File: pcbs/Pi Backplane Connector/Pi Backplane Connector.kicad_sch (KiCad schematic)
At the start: 66 parts, among them J1001 Conn_02x20_Odd_Even, J1002 Conn_02x20_Odd_Even

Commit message: Some routing
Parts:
- added D1033, D1034, D1035, D1036, D1037, D1038, D1039, D1040, D1041, D1042, D1043, D1044, D1045, D1046, D1047, D1048: White, LED_SMD:LED_0603_1608Metric, symbol Device:LED
- added R1033, R1034, R1035, R1036, R1037, R1038, R1039, R1040, R1041, R1042, R1043, R1044, R1045, R1046, R1047, R1048: 4.7k, Resistor_SMD:R_0603_1608Metric, symbol Device:R
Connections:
- net C0: now also J1002.1 (Pin_1), R1033.1; no longer J1002.17 (Pin_17)
- net C1: now also J1002.2 (Pin_2), R1034.1; no longer J1002.18 (Pin_18)
- net C10: now also J1002.11 (Pin_11), R1043.1; no longer J1002.27 (Pin_27)
- net C11: now also J1002.12 (Pin_12), R1044.1; no longer J1002.28 (Pin_28)
- net C12: now also J1002.13 (Pin_13), R1045.1; no longer J1002.29 (Pin_29)
- net C13: now also J1002.14 (Pin_14), R1046.1; no longer J1002.30 (Pin_30)
- net C14: now also J1002.15 (Pin_15), R1047.1; no longer J1002.31 (Pin_31)
- net C15: now also J1002.16 (Pin_16), R1048.1; no longer J1002.32 (Pin_32)
- net C2: now also J1002.3 (Pin_3), R1035.1; no longer J1002.19 (Pin_19)
- net C3: now also J1002.4 (Pin_4), R1036.1; no longer J1002.20 (Pin_20)
- net C4: now also J1002.5 (Pin_5), R1037.1; no longer J1002.21 (Pin_21)
- net C5: now also J1002.6 (Pin_6), R1038.1; no longer J1002.22 (Pin_22)
- net C6: now also J1002.7 (Pin_7), R1039.1; no longer J1002.23 (Pin_23)
- net C7: now also J1002.8 (Pin_8), R1040.1; no longer J1002.24 (Pin_24)
- net C8: now also J1002.9 (Pin_9), R1041.1; no longer J1002.25 (Pin_25)
- net C9: now also J1002.10 (Pin_10), R1042.1; no longer J1002.26 (Pin_26)
- net GND: now also D1033.1 (K), D1034.1 (K), D1035.1 (K), D1036.1 (K), D1037.1 (K), D1038.1 (K), D1039.1 (K), D1040.1 (K), D1041.1 (K), D1042.1 (K), D1043.1 (K), D1044.1 (K), D1045.1 (K), D1046.1 (K), D1047.1 (K), D1048.1 (K)
- net I0: now also J1002.17 (Pin_17); no longer J1002.1 (Pin_1)
- net I1: now also J1002.18 (Pin_18); no longer J1002.2 (Pin_2)
- net I10: now also J1002.27 (Pin_27); no longer J1002.11 (Pin_11)
- net I11: now also J1002.28 (Pin_28); no longer J1002.12 (Pin_12)
- net I12: now also J1002.29 (Pin_29); no longer J1002.13 (Pin_13)
- net I13: now also J1002.30 (Pin_30); no longer J1002.14 (Pin_14)
- net I14: now also J1002.31 (Pin_31); no longer J1002.15 (Pin_15)
- net I15: now also J1002.32 (Pin_32); no longer J1002.16 (Pin_16)
- net I2: now also J1002.19 (Pin_19); no longer J1002.3 (Pin_3)
- net I3: now also J1002.20 (Pin_20); no longer J1002.4 (Pin_4)
- net I4: now also J1002.21 (Pin_21); no longer J1002.5 (Pin_5)
- net I5: now also J1002.22 (Pin_22); no longer J1002.6 (Pin_6)
- net I6: now also J1002.23 (Pin_23); no longer J1002.7 (Pin_7)
- net I7: now also J1002.24 (Pin_24); no longer J1002.8 (Pin_8)
- net I8: now also J1002.25 (Pin_25); no longer J1002.9 (Pin_9)
- net I9: now also J1002.26 (Pin_26); no longer J1002.10 (Pin_10)
- new net: D1034.2 (A), R1034.2
- new net: D1048.2 (A), R1048.2
- new net: D1035.2 (A), R1035.2
- new net: D1037.2 (A), R1037.2
- new net: D1033.2 (A), R1033.2
- new net: D1045.2 (A), R1045.2
- new net: D1043.2 (A), R1043.2
- new net: D1039.2 (A), R1039.2
- new net: D1036.2 (A), R1036.2
- new net: D1044.2 (A), R1044.2
- new net: D1047.2 (A), R1047.2
- new net: D1041.2 (A), R1041.2
- new net: D1040.2 (A), R1040.2
- new net: D1042.2 (A), R1042.2
- new net: D1046.2 (A), R1046.2
- new net: D1038.2 (A), R1038.2
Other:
- sheet Inputs ports: added B[0..15], C[0..15], I[0..15], ~{IN_{LOBD}}; removed none

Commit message: Doing some routing
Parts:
- added D1049, D1050, D1051, D1052, D1053, D1054, D1055, D1056, D1057, D1058, D1059, D1060, D1061, D1062, D1063, D1064: Green, LED_SMD:LED_0603_1608Metric, symbol Device:LED
- added R1049, R1050, R1051, R1052, R1053, R1054, R1055, R1056, R1057, R1058, R1059, R1060, R1061, R1062, R1063, R1064: 4.7k, Resistor_SMD:R_0603_1608Metric, symbol Device:R
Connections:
- net GND: now also D1049.1 (K), D1050.1 (K), D1051.1 (K), D1052.1 (K), D1053.1 (K), D1054.1 (K), D1055.1 (K), D1056.1 (K), D1057.1 (K), D1058.1 (K), D1059.1 (K), D1060.1 (K), D1061.1 (K), D1062.1 (K), D1063.1 (K), D1064.1 (K)
- net I0: now also R1049.1
- net I1: now also R1050.1
- net I10: now also R1059.1
- net I11: now also R1060.1
- net I12: now also R1061.1
- net I13: now also R1062.1
- net I14: now also R1063.1
- net I15: now also R1064.1
- net I2: now also R1051.1
- net I3: now also R1052.1
- net I4: now also R1053.1
- net I5: now also R1054.1
- net I6: now also R1055.1
- net I7: now also R1056.1
- net I8: now also R1057.1
- net I9: now also R1058.1
- new net: D1055.2 (A), R1055.2
- new net: D1057.2 (A), R1057.2
- new net: D1062.2 (A), R1062.2
- new net: D1054.2 (A), R1054.2
- new net: D1061.2 (A), R1061.2
- new net: D1064.2 (A), R1064.2
- new net: D1051.2 (A), R1051.2
- new net: D1063.2 (A), R1063.2
- new net: D1060.2 (A), R1060.2
- new net: D1058.2 (A), R1058.2
- new net: D1049.2 (A), R1049.2
- new net: D1050.2 (A), R1050.2
- new net: D1053.2 (A), R1053.2
- new net: D1052.2 (A), R1052.2
- new net: D1056.2 (A), R1056.2
- new net: D1059.2 (A), R1059.2

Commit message: More connections, more routing
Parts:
- added D1065, D1066, D1067, D1068, D1069: Yellow, LED_SMD:LED_0603_1608Metric, symbol Device:LED
- added R1065, R1066, R1067, R1068, R1069: 4.7k, Resistor_SMD:R_0603_1608Metric, symbol Device:R
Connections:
- net GND: now also D1065.1 (K), D1066.1 (K), D1067.1 (K), D1068.1 (K), D1069.1 (K)
- net Cycle0: now reaches J1002.33 (Pin_33)
- net Cycle0: now also R1065.1
- net Cycle1: now reaches J1002.34 (Pin_34)
- net Cycle1: now also R1066.1
- net Cycle2: now reaches J1002.35 (Pin_35)
- net Cycle2: now also R1067.1
- net Cycle3: now reaches J1002.36 (Pin_36)
- net Cycle3: now also R1068.1
- net Cycle4: now reaches J1002.37 (Pin_37)
- net Cycle4: now also R1069.1
- new net: D1066.2 (A), R1066.2
- new net: D1067.2 (A), R1067.2
- new net: D1065.2 (A), R1065.2
- new net: D1068.2 (A), R1068.2
- new net: D1069.2 (A), R1069.2
- no-connect marks 0 -> 1
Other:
- sheet Inputs ports: added Cycle[0..4]; removed none
- sheet Outputs ports: added Cycle[0..4], DATA, RCLK, SRCLK, ~{Enable_{Cycle}}; removed none

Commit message: Connections and capacitors
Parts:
- added D1070, D1071: Yellow, LED_SMD:LED_0603_1608Metric, symbol Device:LED
- added R1070, R1071: 4.7k, Resistor_SMD:R_0603_1608Metric, symbol Device:R
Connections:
- net GND: now also D1070.1 (K), D1071.1 (K)
- net RESET: now reaches J1001.39 (Pin_39)
- net RESET: now also R1071.1
- net CLOCK: now reaches J1001.40 (Pin_40)
- net CLOCK: now also R1070.1
- new net: D1071.2 (A), R1071.2
- new net: D1070.2 (A), R1070.2
- no-connect marks 1 -> 5
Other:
- sheet Inputs ports: added CLOCK, RESET; removed none
- sheet Outputs ports: added CLOCK, RESET, ~{CLOCK_{enable}}, ~{Cycle_{enable}}, ~{RESET_{enable}}; removed ~{Enable_{Cycle}}

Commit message: Thinking about Pi connections
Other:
- sheet Inputs ports: added none; removed ~{IN_{LOBD}}
- sheet Pi Control ports: added CLK_IN, CLK_OUT, DATA_OUT, IN_DATA, ~{A_{en}}, ~{B_{en}}, ~{CLOCK_{en}}, ~{CYCLE_{en}}, ~{C_{en}}, ~{IN_{en}}, ~{IN_{ld}}, ~{I_{en}}, ~{OUT_{en}}, ~{RESET_{en}}; removed none

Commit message: Doing some routing
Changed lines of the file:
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@@
 		)
 		(pin "~{OUT_{en}}" output
-			(at 102.87 58.42 0)
+			(at 102.87 24.13 0)
 			(effects
 				(font
@@
 		)
 		(pin "~{IN_{en}}" output
-			(at 102.87 24.13 0)
+			(at 102.87 58.42 0)
 			(effects
 				(font

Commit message: Double checking
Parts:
- added H1001, H1002, H1003, H1004: MountingHole, MountingHole:MountingHole_2.7mm_M2.5_ISO7380, symbol Mechanical:MountingHole

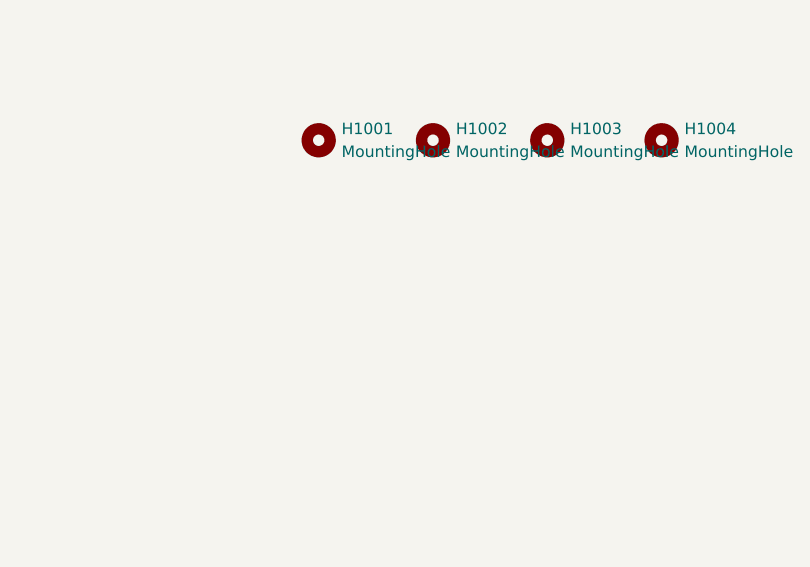
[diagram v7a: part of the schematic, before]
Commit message: Add barrel connector
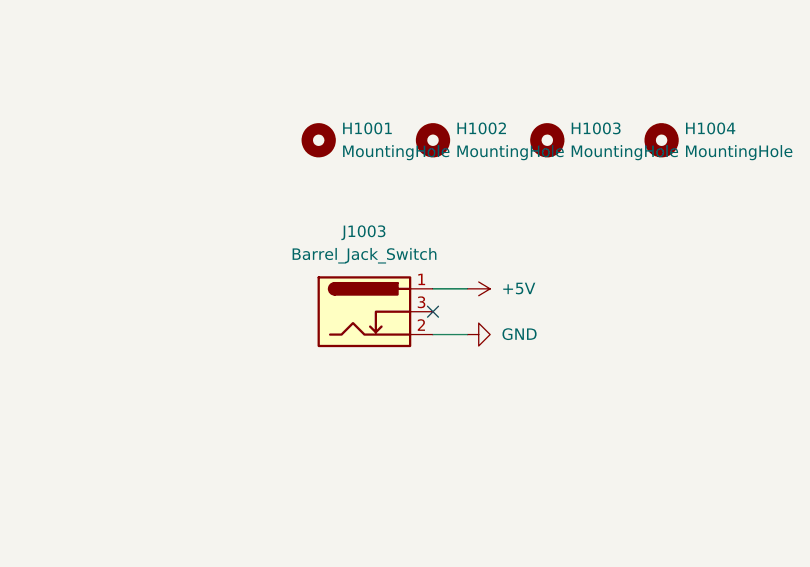
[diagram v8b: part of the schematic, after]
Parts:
- added J1003: Barrel_Jack_Switch, Connector_BarrelJack:BarrelJack_Horizontal, symbol Connector:Barrel_Jack_Switch
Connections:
- net +5V: now also J1003.1
- net GND: now also J1003.2
- no-connect marks 5 -> 6
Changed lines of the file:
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@@
 	)
 	(no_connect
+		(at 292.1 234.95)
+	)
+	(no_connect
 		(at 342.9 92.71)
 	)
@@
 		)
 	)
+	(wire
+		(pts
+			(xy 292.1 232.41) (xy 295.91 232.41)
+		)
+		(stroke
+			(width 0)
+			(type default)
+		)
+	)
 	(bus
 		(pts
@@
 	(wire
 		(pts
+			(xy 292.1 237.49) (xy 295.91 237.49)
+		)
+		(stroke
+			(width 0)
+			(type default)
+		)
+	)
+	(wire
+		(pts
 			(xy 38.1 135.89) (xy 38.1 139.7)
 		)
@@
 	)
 	(symbol
+		(lib_id "Connector:Barrel_Jack_Switch")
+		(at 284.48 234.95 0)
+		(unit 1)
+		(exclude_from_sim no)
+		(in_bom yes)
+		(on_board yes)
+		(dnp no)
+		(fields_autoplaced yes)
+		(property "Reference" "J1003"
+			(at 284.48 226.06 0)
+			(effects
+				(font
+					(size 1.27 1.27)
+				)
+			)
+		)
+		(property "Value" "Barrel_Jack_Switch"
+			(at 284.48 228.6 0)
+			(effects
+				(font
+					(size 1.27 1.27)
+				)
+			)
+		)
+		(property "Footprint" "Connector_BarrelJack:BarrelJack_Horizontal"
+			(at 285.75 235.966 0)
+			(effects
+				(font
+					(size 1.27 1.27)
+				)
+				(hide yes)
+			)
+		)
+		(property "Datasheet" "~"
+			(at 285.75 235.966 0)
+			(effects
+				(font
+					(size 1.27 1.27)
+				)
+				(hide yes)
+			)
+		)
+		(property "Description" "DC Barrel Jack with an internal switch"
+			(at 284.48 234.95 0)
+			(effects
+				(font
+					(size 1.27 1.27)
+				)
+				(hide yes)
+			)
+		)
+		(pin "1"
+		)
+		(pin "2"
+		)
+		(pin "3"
+		)
+		(instances
+			(project "Pi Backplane Connector"
+				(path "/84ab2617-954b-4ceb-a5e3-268c9e11a862"
+					(reference "J1003")
+					(unit 1)
+				)
+			)
+		)
+	)
+	(symbol
 		(lib_id "Device:LED")
 		(at 127 207.01 90)
@@
 	)
 	(symbol
+		(lib_name "+5V_1")
+		(lib_id "power:+5V")
+		(at 295.91 232.41 270)
+		(unit 1)
+		(exclude_from_sim no)
+		(in_bom yes)
+		(on_board yes)
+		(dnp no)
+		(fields_autoplaced yes)
+		(property "Reference" "#PWR01011"
+			(at 292.1 232.41 0)
+			(effects
+				(font
+					(size 1.27 1.27)
+				)
+				(hide yes)
+			)
+		)
+		(property "Value" "+5V"
+			(at 299.72 232.4099 90)
+			(effects
+				(font
+					(size 1.27 1.27)
+				)
+				(justify left)
+			)
+		)
+		(property "Footprint" ""
+			(at 295.91 232.41 0)
+			(effects
+				(font
+					(size 1.27 1.27)
+				)
+				(hide yes)
+			)
+		)
+		(property "Datasheet" ""
+			(at 295.91 232.41 0)
+			(effects
+				(font
+					(size 1.27 1.27)
+				)
+				(hide yes)
+			)
+		)
+		(property "Description" "Power symbol creates a global label with name \"+5V\""
+			(at 295.91 232.41 0)
+			(effects
+				(font
+					(size 1.27 1.27)
+				)
+				(hide yes)
+			)
+		)
+		(pin "1"
+		)
+		(instances
+			(project "Pi Backplane Connector"
+				(path "/84ab2617-954b-4ceb-a5e3-268c9e11a862"
+					(reference "#PWR01011")
+					(unit 1)
+				)
+			)
+		)
+	)
+	(symbol
 		(lib_id "Device:LED")
 		(at 101.6 156.21 90)
@@
 					(unit 1)
 				)
+			)
+		)
+	)
+	(symbol
+		(lib_name "GND_1")
+		(lib_id "power:GND")
+		(at 295.91 237.49 90)
+		(unit 1)
+		(exclude_from_sim no)
+		(in_bom yes)
+		(on_board yes)
+		(dnp no)
+		(fields_autoplaced yes)
+		(property "Reference" "#PWR01012"
+			(at 302.26 237.49 0)
+			(effects
+				(font
+					(size 1.27 1.27)
+				)
+				(hide yes)
+			)
+		)
+		(property "Value" "GND"
+			(at 299.72 237.4899 90)
+			(effects
+				(font
+					(size 1.27 1.27)
+				)
+				(justify right)
+			)
+		)
+		(property "Footprint" ""
+			(at 295.91 237.49 0)
+			(effects
+				(font
+					(size 1.27 1.27)
+				)
+				(hide yes)
+			)
+		)
+		(property "Datasheet" ""
+			(at 295.91 237.49 0)
+			(effects
+				(font
+					(size 1.27 1.27)
+				)
+				(hide yes)
+			)
+		)
+		(property "Description" "Power symbol creates a global label with name \"GND\" , ground"
+			(at 295.91 237.49 0)
+			(effects
+				(font
+					(size 1.27 1.27)
+				)
+				(hide yes)
+			)
+		)
+		(pin "1"
+		)
+		(instances
+			(project "Pi Backplane Connector"
+				(path "/84ab2617-954b-4ceb-a5e3-268c9e11a862"
+					(reference "#PWR01012")
+					(unit 1)
+				)
